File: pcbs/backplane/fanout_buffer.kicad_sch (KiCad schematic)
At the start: 14 parts

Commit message: Schematic file fix, misc. PCB
Fixed issue with KiCAD's automatic V5→V6 migration (corrected in 6.0.11) that caused problems with component references in multi-channel schematic sheets
Finished migration in amp ctrl PCB, inc. re-assigning "exclude from BOM" attributes to testpoints, solder jumpers
Added mounting hole to amp ctrl PCB for addl support to Ethernet jacks, power connector through stiffener
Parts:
- C? (x5): renamed from ?; value 100nF 50V X7R -> (none); footprint Capacitor_SMD:C_0603_1608Metric -> (none)
- C?: renamed from ?; value 1uF 50V X7R -> (none); footprint Capacitor_SMD:C_0805_2012Metric -> (none)
- JP? (x5): renamed from ?; value Jumper_NC_Small -> (none); footprint Jumper:SolderJumper-2_P1.3mm_Bridged_RoundedPad1.0x1.5mm -> (none)
- JP?: renamed from ?; value Jumper_NC_Small -> (none); footprint Jumper:SolderJumper-2_P1.3mm_Open_TrianglePad1.0x1.5mm -> (none)
- R1: renamed from ?; value 100 -> (none); footprint Resistor_SMD:R_0402_1005Metric -> (none)
- U?: renamed from ?; value CDCUN1208LP -> (none); footprint Martinos:VQFN-32-1EP_5x5mm_P0.5mm_EP3.45x3.45mm -> (none)

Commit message: Amp ctrl: lengthened ADC & DAC reset delay to ~50 ms (#14) Backplane: added clock multiplier for 10 Mhz scanner clock (fixes #21) Backplane: reduced R5 from 10 to 1 ohm, to avoid excessive voltage drop (#20) Backplane: replaced 15V regulator with efficient voltage limiter (#20) Backplane: changed all mounting holes to signal ground Backplane: replaced +2.5V regulator with a higher-current model to support FPGA I/O bank current draw Updated to KiCAD 8
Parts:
- C36: renamed from C?; value (none) -> 1uF 50V X7R; footprint (none) -> Capacitor_SMD:C_0805_2012Metric
- C5, C6, C7, C8, C9: renamed from C?; value (none) -> 100nF 50V X7R; footprint (none) -> Capacitor_SMD:C_0603_1608Metric
- JP1: renamed from JP?; value (none) -> Jumper_NC_Small; footprint (none) -> Jumper:SolderJumper-2_P1.3mm_Open_TrianglePad1.0x1.5mm
- JP2, JP3, JP4, JP5, JP6: renamed from JP?; value (none) -> Jumper_NC_Small; footprint (none) -> Jumper:SolderJumper-2_P1.3mm_Bridged_RoundedPad1.0x1.5mm
- R1: value (none) -> 100; footprint (none) -> Resistor_SMD:R_0402_1005Metric
- U2: renamed from U?; value (none) -> CDCUN1208LP; footprint (none) -> Martinos:VQFN-32-1EP_5x5mm_P0.5mm_EP3.45x3.45mm

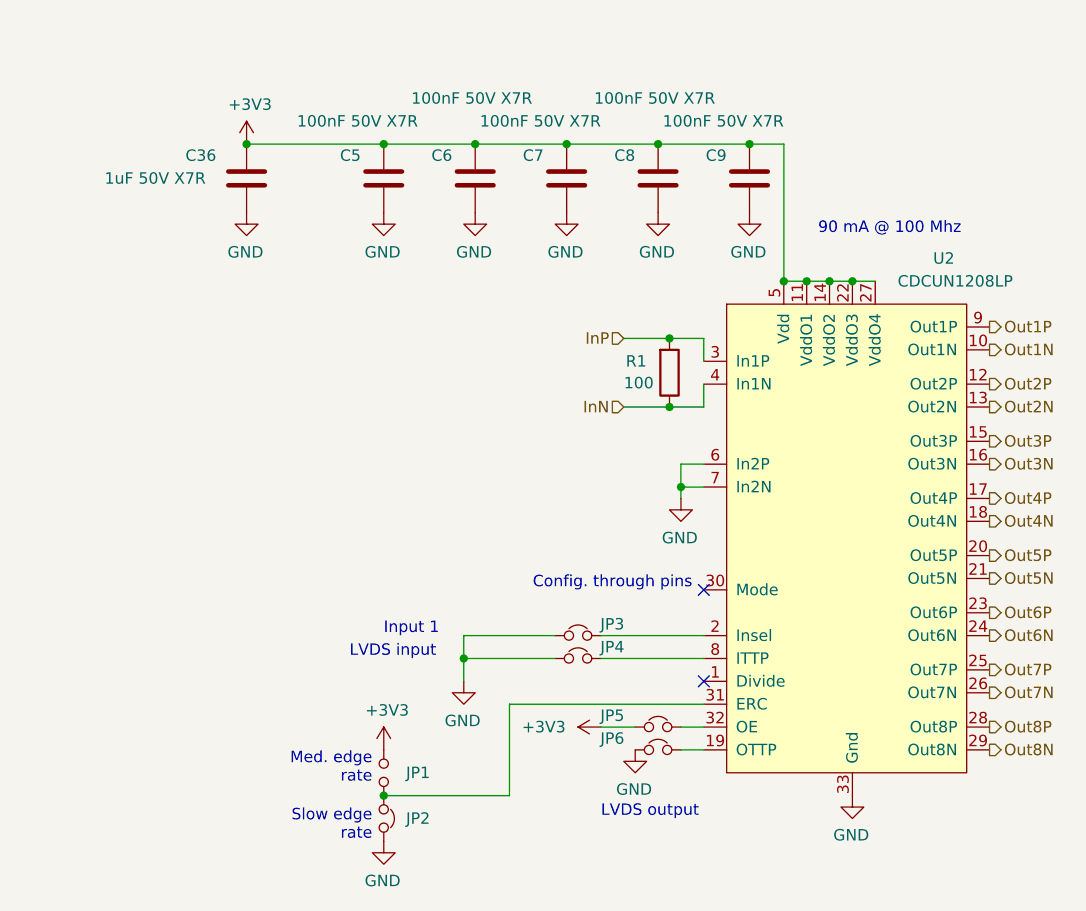
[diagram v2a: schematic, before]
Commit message: Corrected power-up behavior
Backplane: Inverted polarity of Shutdown_Force (now Power_Enable_FPGA), to keep amps powered off until software starts: fixes #23
Backplane: Routed Shutdown_Force to unused pin 3 on RJ45 jack B to amp boards: fixes #23
Backplane: Added pull-up and pull-down resistors to fanout buffer inputs, to keep SCK & ~LDAC signals in proper state during power-on: fixes #23
Amp control: Added transistor to reset DAC & ADC from pin 3 of RJ45 jack B
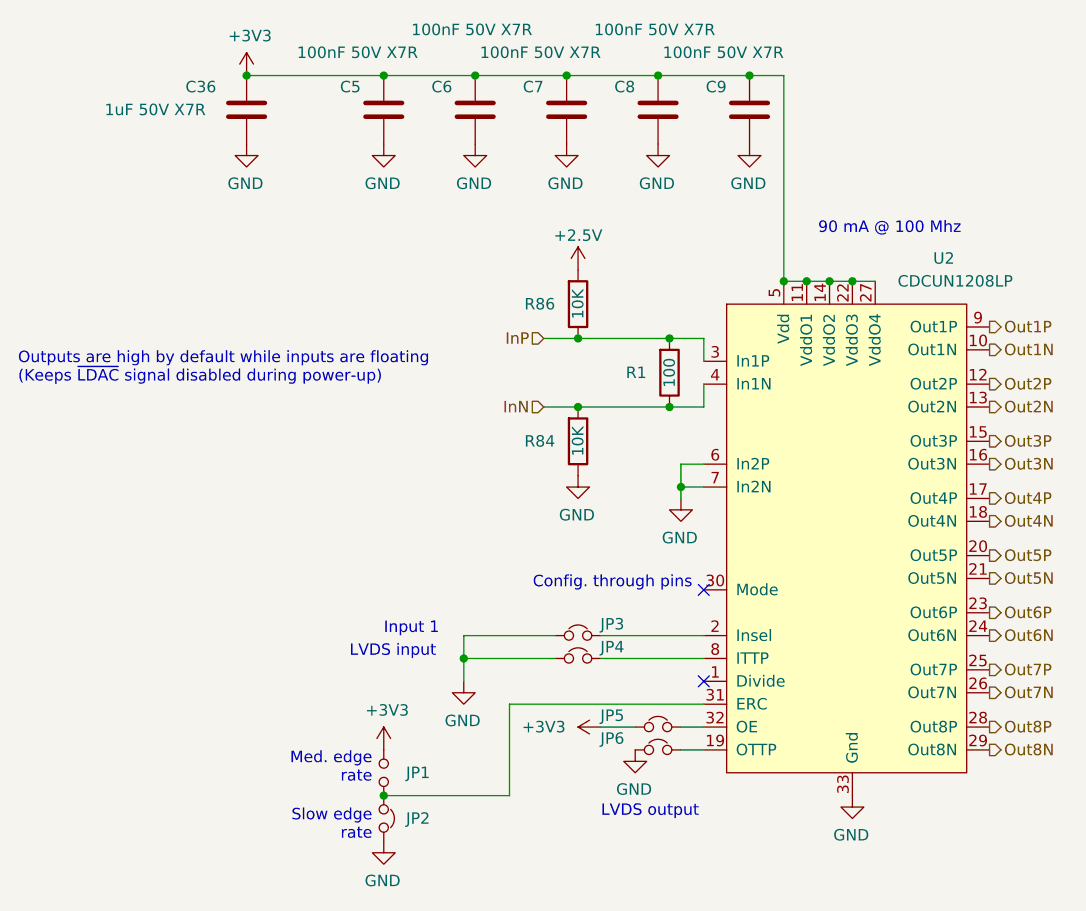
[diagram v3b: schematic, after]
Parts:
- added R84, R86: 10K, Resistor_SMD:R_0402_1005Metric, symbol Device:R
- U2: footprint Martinos:VQFN-32-1EP_5x5mm_P0.5mm_EP3.45x3.45mm -> Don:VQFN-32-1EP_5x5mm_P0.5mm_EP3.45x3.45mm
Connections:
- net GND: now also R84.1
- net InN: now also R84.2
- net InP: now also R86.1
- new net +2.5V: R86.2
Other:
- note added: "Outputs are high by default while inputs are floating (Keeps ~{LDAC} signal disabled during power-up)"
- moved on the sheet: C36, C5, C6, C7, C8, C9

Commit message: Misc. cleanup for mfg & improvements
Minor backplane pinout doc corrections (SCKO5 polarity, clarified some descriptions)
Backplane: Added differential- and common-mode (to standoffs) power filtering, for EMI escaping over power wiring
Amp ctrl: Changed DAC testpoints from individual pads to Keystone 5019 for easier probing
Corrected part numbers, DNP vs. non-BOM-item indications, other misc. BOM issues
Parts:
- JP1: value Jumper_NC_Small -> Jumper_NO_Small; now left out of the parts list
- JP2, JP3, JP4, JP5, JP6: now left out of the parts list
- R84, R86: Part Number RK73H1ETTP1000F -> RK73H1ETTP1002F
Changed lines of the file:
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@@
 		(unit 1)
 		(exclude_from_sim no)
-		(in_bom yes)
+		(in_bom no)
 		(on_board yes)
 		(dnp no)
@@
 		(unit 1)
 		(exclude_from_sim no)
-		(in_bom yes)
+		(in_bom no)
 		(on_board yes)
 		(dnp no)
@@
 		(unit 1)
 		(exclude_from_sim no)
-		(in_bom yes)
+		(in_bom no)
 		(on_board yes)
 		(dnp no)
@@
 		(unit 1)
 		(exclude_from_sim no)
-		(in_bom yes)
+		(in_bom no)
 		(on_board yes)
 		(dnp no)
@@
 		(unit 1)
 		(exclude_from_sim no)
-		(in_bom yes)
+		(in_bom no)
 		(on_board yes)
 		(dnp no)
@@
 		(unit 1)
 		(exclude_from_sim no)
-		(in_bom yes)
+		(in_bom no)
 		(on_board yes)
 		(dnp no)
@@
 			)
 		)
-		(property "Value" "Jumper_NC_Small"
+		(property "Value" "Jumper_NO_Small"
 			(at 97.0534 121.92 0)
 			(effects
@@
 			)
 		)
-		(property "Part Number" "RK73H1ETTP1000F"
+		(property "Part Number" "RK73H1ETTP1002F"
 			(at 115.57 69.85 0)
 			(effects
@@
 			)
 		)
-		(property "Part Number" "RK73H1ETTP1000F"
+		(property "Part Number" "RK73H1ETTP1002F"
 			(at 115.57 85.09 0)
 			(effects

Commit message: Updated KiCAD file versions to 9.0
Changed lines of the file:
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@@
 (kicad_sch
-	(version 20231120)
+	(version 20250114)
 	(generator "eeschema")
-	(generator_version "8.0")
+	(generator_version "9.0")
 	(paper "A4")
 	(title_block
@@
 		(comment 1 "Don Straney")
 	)
+	(text "LVDS input"
+		(exclude_from_sim no)
+		(at 90.17 109.22 0)
+		(effects
+			(font
+				(size 1.27 1.27)
+			)
+			(justify left bottom)
+		)
+	)
+	(text "Slow edge\nrate"
+		(exclude_from_sim no)
+		(at 92.71 129.54 0)
+		(effects
+			(font
+				(size 1.27 1.27)
+			)
+			(justify right bottom)
+		)
+	)
+	(text "Input 1"
+		(exclude_from_sim no)
+		(at 93.98 106.68 0)
+		(effects
+			(font
+				(size 1.27 1.27)
+			)
+			(justify left bottom)
+		)
+	)
+	(text "LVDS output"
+		(exclude_from_sim no)
+		(at 118.11 127 0)
+		(effects
+			(font
+				(size 1.27 1.27)
+			)
+			(justify left bottom)
+		)
+	)
+	(text "Outputs are high by default while inputs are floating\n(Keeps ~{LDAC} signal disabled during power-up)"
+		(exclude_from_sim no)
+		(at 53.34 78.74 0)
+		(effects
+			(font
+				(size 1.27 1.27)
+			)
+			(justify left bottom)
+		)
+	)
+	(text "Med. edge\nrate"
+		(exclude_from_sim no)
+		(at 92.71 123.19 0)
+		(effects
+			(font
+				(size 1.27 1.27)
+			)
+			(justify right bottom)
+		)
+	)
+	(text "Config. through pins"
+		(exclude_from_sim no)
+		(at 128.27 101.6 0)
+		(effects
+			(font
+				(size 1.27 1.27)
+			)
+			(justify right bottom)
+		)
+	)
+	(text "90 mA @ 100 Mhz"
+		(exclude_from_sim no)
+		(at 142.24 62.23 0)
+		(effects
+			(font
+				(size 1.27 1.27)
+			)
+			(justify left bottom)
+		)
+	)
 	(junction
 		(at 102.87 109.22)
@@
 		)
 	)
-	(text "LVDS input"
-		(exclude_from_sim no)
-		(at 90.17 109.22 0)
-		(effects
-			(font
-				(size 1.27 1.27)
-			)
-			(justify left bottom)
-		)
-	)
-	(text "Slow edge\nrate"
-		(exclude_from_sim no)
-		(at 92.71 129.54 0)
-		(effects
-			(font
-				(size 1.27 1.27)
-			)
-			(justify right bottom)
-		)
-	)
-	(text "Input 1"
-		(exclude_from_sim no)
-		(at 93.98 106.68 0)
-		(effects
-			(font
-				(size 1.27 1.27)
-			)
-			(justify left bottom)
-		)
-	)
-	(text "LVDS output"
-		(exclude_from_sim no)
-		(at 118.11 127 0)
-		(effects
-			(font
-				(size 1.27 1.27)
-			)
-			(justify left bottom)
-		)
-	)
-	(text "Outputs are high by default while inputs are floating\n(Keeps ~{LDAC} signal disabled during power-up)"
-		(exclude_from_sim no)
-		(at 53.34 78.74 0)
-		(effects
-			(font
-				(size 1.27 1.27)
-			)
-			(justify left bottom)
-		)
-	)
-	(text "Med. edge\nrate"
-		(exclude_from_sim no)
-		(at 92.71 123.19 0)
-		(effects
-			(font
-				(size 1.27 1.27)
-			)
-			(justify right bottom)
-		)
-	)
-	(text "Config. through pins"
-		(exclude_from_sim no)
-		(at 128.27 101.6 0)
-		(effects
-			(font
-				(size 1.27 1.27)
-			)
-			(justify right bottom)
-		)
-	)
-	(text "90 mA @ 100 Mhz"
-		(exclude_from_sim no)
-		(at 142.24 62.23 0)
-		(effects
-			(font
-				(size 1.27 1.27)
-			)
-			(justify left bottom)
-		)
-	)

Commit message: Moved all project-specific symbols & footprints into new "shim" libraries Updated projects to reference the new "shim" library
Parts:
- U2: footprint Don:VQFN-32-1EP_5x5mm_P0.5mm_EP3.45x3.45mm -> shim:VQFN-32-1EP_5x5mm_P0.5mm_EP3.45x3.45mm
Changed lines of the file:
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@@
 			)
 		)
-		(property "Footprint" "Don:VQFN-32-1EP_5x5mm_P0.5mm_EP3.45x3.45mm"
+		(property "Footprint" "shim:VQFN-32-1EP_5x5mm_P0.5mm_EP3.45x3.45mm"
 			(at 154.94 68.58 0)
 			(effects
